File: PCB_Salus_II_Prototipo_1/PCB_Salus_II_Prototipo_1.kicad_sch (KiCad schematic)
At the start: 52 parts, among them J1 Servo1, J10 Conn_01x07_Pin, J11 Conector Entrada 5V, J12 Conector 5V, J13 Conector Entrada 7V, J14 Conector Salida 7V, J15 Sensor 1, J16 Luz2, J17 Cambios1, J18 Cambios 2, J19 MarchaAtras1, J2 Sensor Giro, J20 MarchaAtras2, J21 Sobrante1, J22 Sobrante2, J23 Arranque1, J24 Arranque2, J25 ControlMotor, J26 Sensor 2, J27 Sensor 3, J28 Sensor 4, J29 Sensor 5, J3 Acelerador, J30 Sensor 6, J31 Sensor 7, J4 Conn_01x05_Pin, J5 Servo2, J6 Antena, J7 SensorGiro, J8 Luz1, J9 Conn_01x07_Pin, K1 Rele 5V, K2 Rele 7V, K3 Arranque, Q1 IO25, Q2 IO26, Q3 IO27, Q4 IO14, U1 ESP32-DEVKITC-32D, U2 RASPBERRY_PI_4B_4GB

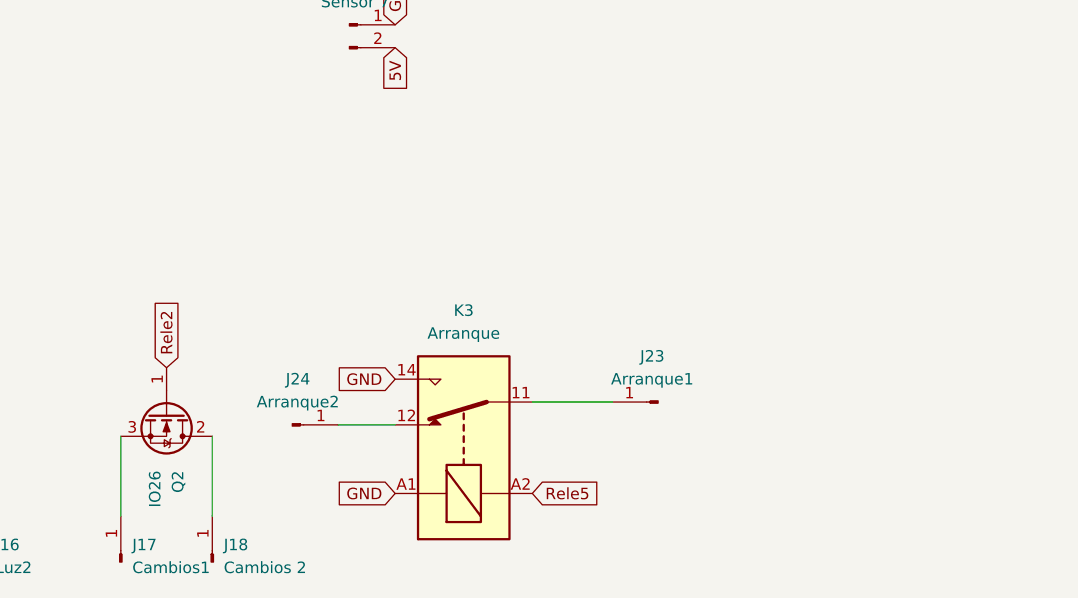
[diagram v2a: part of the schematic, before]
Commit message: Se realizaron cambios de conexion de rele en Kicad
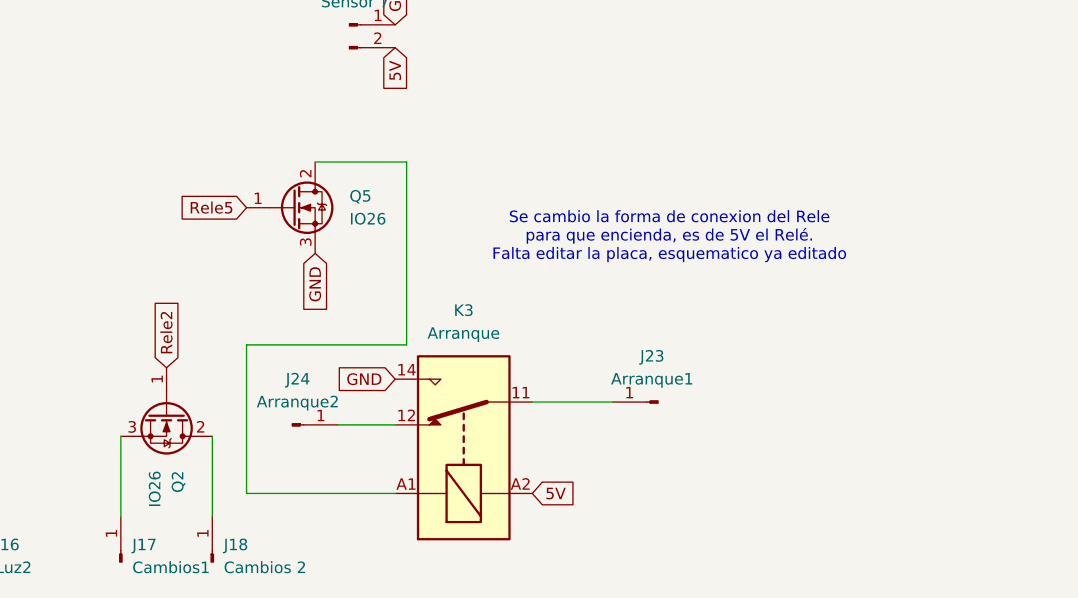
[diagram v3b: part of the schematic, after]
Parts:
- added Q5: IO26, Package_TO_SOT_THT:TO-220-3_Vertical, symbol Transistor_FET:IRLZ44N
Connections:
- net 5V: now also K3.A2
- net GND: now also Q5.3 (S); no longer K3.A1
- net Rele5: now also Q5.1 (G); no longer K3.A2
- new net: K3.A1, Q5.2 (D)
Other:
- note added: "Se cambio la forma de conexion del Rele para que encienda, es de 5V el Relé. Falta editar la placa, esquematico ya editado"
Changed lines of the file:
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@@
 	(wire
 		(pts
+			(xy 124.46 160.02) (xy 142.24 160.02)
+		)
+		(stroke
+			(width 0)
+			(type default)
+		)
+	)
+	(wire
+		(pts
 			(xy 95.25 170.18) (xy 95.25 179.07)
 		)
@@
 	(wire
 		(pts
+			(xy 142.24 139.7) (xy 132.08 139.7)
+		)
+		(stroke
+			(width 0)
+			(type default)
+		)
+	)
+	(wire
+		(pts
+			(xy 142.24 160.02) (xy 142.24 139.7)
+		)
+		(stroke
+			(width 0)
+			(type default)
+		)
+	)
+	(wire
+		(pts
+			(xy 140.97 176.53) (xy 124.46 176.53)
+		)
+		(stroke
+			(width 0)
+			(type default)
+		)
+	)
+	(wire
+		(pts
 			(xy 203.2 20.32) (xy 203.2 19.05)
 		)
@@
 	(wire
 		(pts
+			(xy 124.46 176.53) (xy 124.46 160.02)
+		)
+		(stroke
+			(width 0)
+			(type default)
+		)
+	)
+	(wire
+		(pts
 			(xy 53.34 167.64) (xy 53.34 176.53)
 		)
@@
 		)
 	)
+	(text "Se cambio la forma de conexion del Rele \npara que encienda, es de 5V el Relé.\nFalta editar la placa, esquematico ya editado\n"
+		(exclude_from_sim no)
+		(at 171.45 148.082 0)
+		(effects
+			(font
+				(size 1.27 1.27)
+			)
+		)
+	)
 	(text "SISTEMA SEGURIDAD 5V\n"
 		(exclude_from_sim no)
@@
 		)
 	)
-	(global_label "3V3"
+	(global_label "Rele5"
 		(shape input)
-		(at 269.24 54.61 270)
+		(at 124.46 144.78 180)
 		(fields_autoplaced yes)
 		(effects
@@
 		)
 		(property "Intersheetrefs" "${INTERSHEET_REFS}"
-			(at 269.24 61.1028 90)
+			(at 116.1529 144.78 0)
 			(effects
 				(font
@@
 		)
 	)
-	(global_label "GND"
+	(global_label "3V3"
 		(shape input)
-		(at 231.14 45.72 0)
+		(at 269.24 54.61 270)
 		(fields_autoplaced yes)
 		(effects
@@
 				(size 1.27 1.27)
 			)
-			(justify left)
+			(justify right)
 		)
 		(property "Intersheetrefs" "${INTERSHEET_REFS}"
-			(at 237.9957 45.72 0)
+			(at 269.24 61.1028 90)
 			(effects
 				(font
 					(size 1.27 1.27)
 				)
-				(justify left)
+				(justify right)
 				(hide yes)
 			)
 		)
 	)
-	(global_label "Rele5"
+	(global_label "GND"
 		(shape input)
-		(at 156.21 176.53 0)
+		(at 231.14 45.72 0)
 		(fields_autoplaced yes)
 		(effects
@@
 		)
 		(property "Intersheetrefs" "${INTERSHEET_REFS}"
-			(at 164.5171 176.53 0)
+			(at 237.9957 45.72 0)
 			(effects
 				(font
@@
 		)
 	)
+	(global_label "5V"
+		(shape input)
+		(at 156.21 176.53 0)
+		(fields_autoplaced yes)
+		(effects
+			(font
+				(size 1.27 1.27)
+			)
+			(justify left)
+		)
+		(property "Intersheetrefs" "${INTERSHEET_REFS}"
+			(at 161.4933 176.53 0)
+			(effects
+				(font
+					(size 1.27 1.27)
+				)
+				(justify left)
+				(hide yes)
+			)
+		)
+	)
 	(global_label "GND"
 		(shape input)
@@
 		)
 	)
-	(global_label "Acelerador"
+	(global_label "GND"
 		(shape input)
-		(at 109.22 52.07 270)
+		(at 132.08 149.86 270)
 		(fields_autoplaced yes)
 		(effects
@@
 		)
 		(property "Intersheetrefs" "${INTERSHEET_REFS}"
-			(at 109.22 65.0942 90)
+			(at 132.08 156.7157 90)
 			(effects
 				(font
@@
 		)
 	)
-	(global_label "GND"
+	(global_label "Acelerador"
 		(shape input)
-		(at 111.76 52.07 0)
+		(at 109.22 52.07 270)
 		(fields_autoplaced yes)
 		(effects
@@
 				(size 1.27 1.27)
 			)
-			(justify left)
+			(justify right)
 		)
 		(property "Intersheetrefs" "${INTERSHEET_REFS}"
-			(at 118.6157 52.07 0)
+			(at 109.22 65.0942 90)
 			(effects
 				(font
 					(size 1.27 1.27)
 				)
-				(justify left)
+				(justify right)
 				(hide yes)
 			)
 		)
 	)
-	(global_label "Rele5"
+	(global_label "GND"
 		(shape input)
-		(at 73.66 111.76 0)
+		(at 111.76 52.07 0)
 		(fields_autoplaced yes)
 		(effects
@@
 		)
 		(property "Intersheetrefs" "${INTERSHEET_REFS}"
-			(at 81.9671 111.76 0)
+			(at 118.6157 52.07 0)
 			(effects
 				(font
@@
 		)
 	)
-	(global_label "GND"
+	(global_label "Rele5"
 		(shape input)
-		(at 140.97 176.53 180)
+		(at 73.66 111.76 0)
 		(fields_autoplaced yes)
 		(effects
@@
 				(size 1.27 1.27)
 			)
-			(justify right)
+			(justify left)
 		)
 		(property "Intersheetrefs" "${INTERSHEET_REFS}"
-			(at 134.1143 176.53 0)
+			(at 81.9671 111.76 0)
 			(effects
 				(font
 					(size 1.27 1.27)
 				)
-				(justify right)
+				(justify left)
 				(hide yes)
 			)
@@
 					(unit 1)
 				)
+			)
+		)
+	)
+	(symbol
+		(lib_id "Transistor_FET:IRLZ44N")
+		(at 129.54 144.78 0)
+		(unit 1)
+		(exclude_from_sim no)
+		(in_bom yes)
+		(on_board yes)
+		(dnp no)
+		(fields_autoplaced yes)
+		(property "Reference" "Q5"
+			(at 135.89 143.5099 0)
+			(effects
+				(font
+					(size 1.27 1.27)
+				)
+				(justify left)
+			)
+		)
+		(property "Value" "IO26"
+			(at 135.89 146.0499 0)
+			(effects
+				(font
+					(size 1.27 1.27)
+				)
+				(justify left)
+			)
+		)
+		(property "Footprint" "Package_TO_SOT_THT:TO-220-3_Vertical"
+			(at 134.62 146.685 0)
+			(effects
+				(font
+					(size 1.27 1.27)
+					(italic yes)
+				)
+				(justify left)
+				(hide yes)
+			)
+		)
+		(property "Datasheet" "http://www.irf.com/product-info/datasheets/data/irlz44n.pdf"
+			(at 134.62 148.59 0)
+			(effects
+				(font
+					(size 1.27 1.27)
+				)
+				(justify left)
+				(hide yes)
+			)
+		)
+		(property "Description" "47A Id, 55V Vds, 22mOhm Rds Single N-Channel HEXFET Power MOSFET, TO-220AB"
+			(at 129.54 144.78 0)
+			(effects
+				(font
+					(size 1.27 1.27)
+				)
+				(hide yes)
+			)
+		)
+		(pin "2"
+		)
+		(pin "1"
+		)
+		(pin "3"
+		)
+		(instances
+			(project "PCB_Salus_II_Prototipo_1"
+				(path "/ba46b43d-a80c-4bb9-8819-4a9c21f18053"
+					(reference "Q5")
+					(unit 1)
+				)
